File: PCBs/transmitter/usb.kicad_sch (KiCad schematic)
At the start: 4 parts, among them J10 USB_C_Receptacle_USB2.0

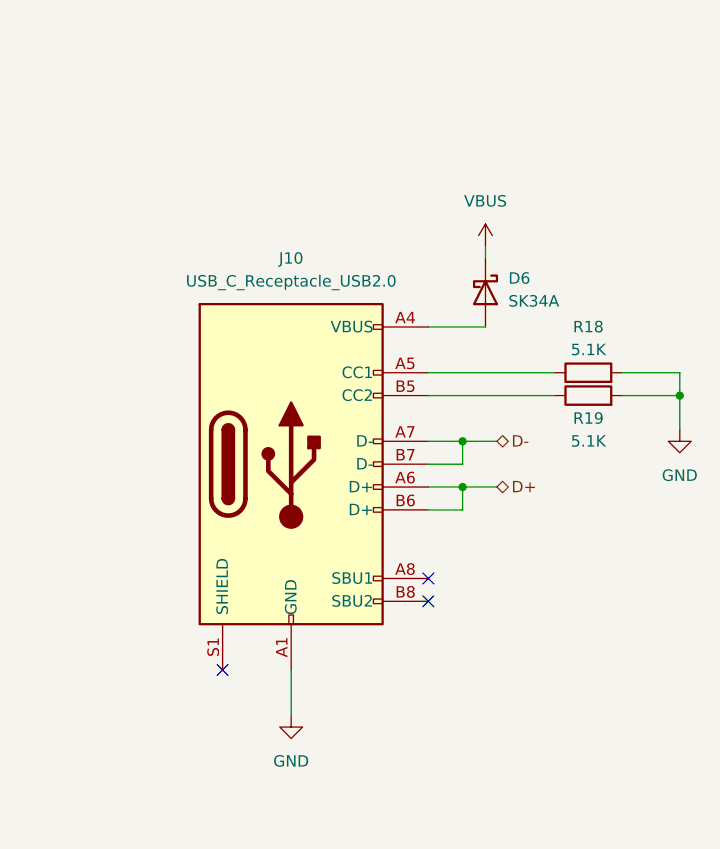
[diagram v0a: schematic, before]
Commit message: updated schematics
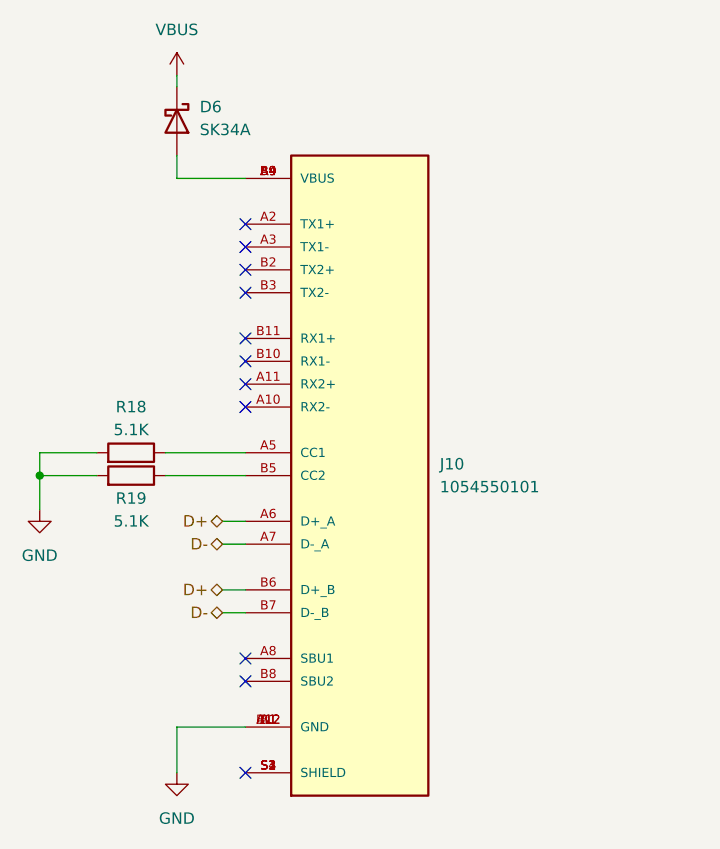
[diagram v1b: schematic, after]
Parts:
- removed J10: USB_C_Receptacle_USB2.0, symbol Connector:USB_C_Receptacle_USB2.0
- added J10: 1054550101, Connector_Molex:MOLEX_1054550101, symbol 1054550101:1054550101
- R18, R19: footprint (none) -> Resistor_SMD:R_0603_1608Metric
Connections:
- net D+: now also J10.A6 (D+_A), J10.B6 (D+_B)
- net D-: now also J10.A7 (D-_A), J10.B7 (D-_B)
- net GND: now also J10.A1 (GND), J10.A12 (GND), J10.B1 (GND), J10.B12 (GND)
- net at D6.2 (A): now also J10.A4 (VBUS), J10.A9 (VBUS), J10.B4 (VBUS), J10.B9 (VBUS)
- net at R18.1: now also J10.A5 (CC1)
- net at R19.1: now also J10.B5 (CC2)
- new net: J10.S1 (SHIELD), J10.S2 (SHIELD), J10.S3 (SHIELD), J10.S4 (SHIELD)
- no-connect marks 3 -> 11
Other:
- moved on the sheet: D6
